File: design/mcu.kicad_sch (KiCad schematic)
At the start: 13 parts, among them U1 STM32F40X_LQFP64, X1 8MHz

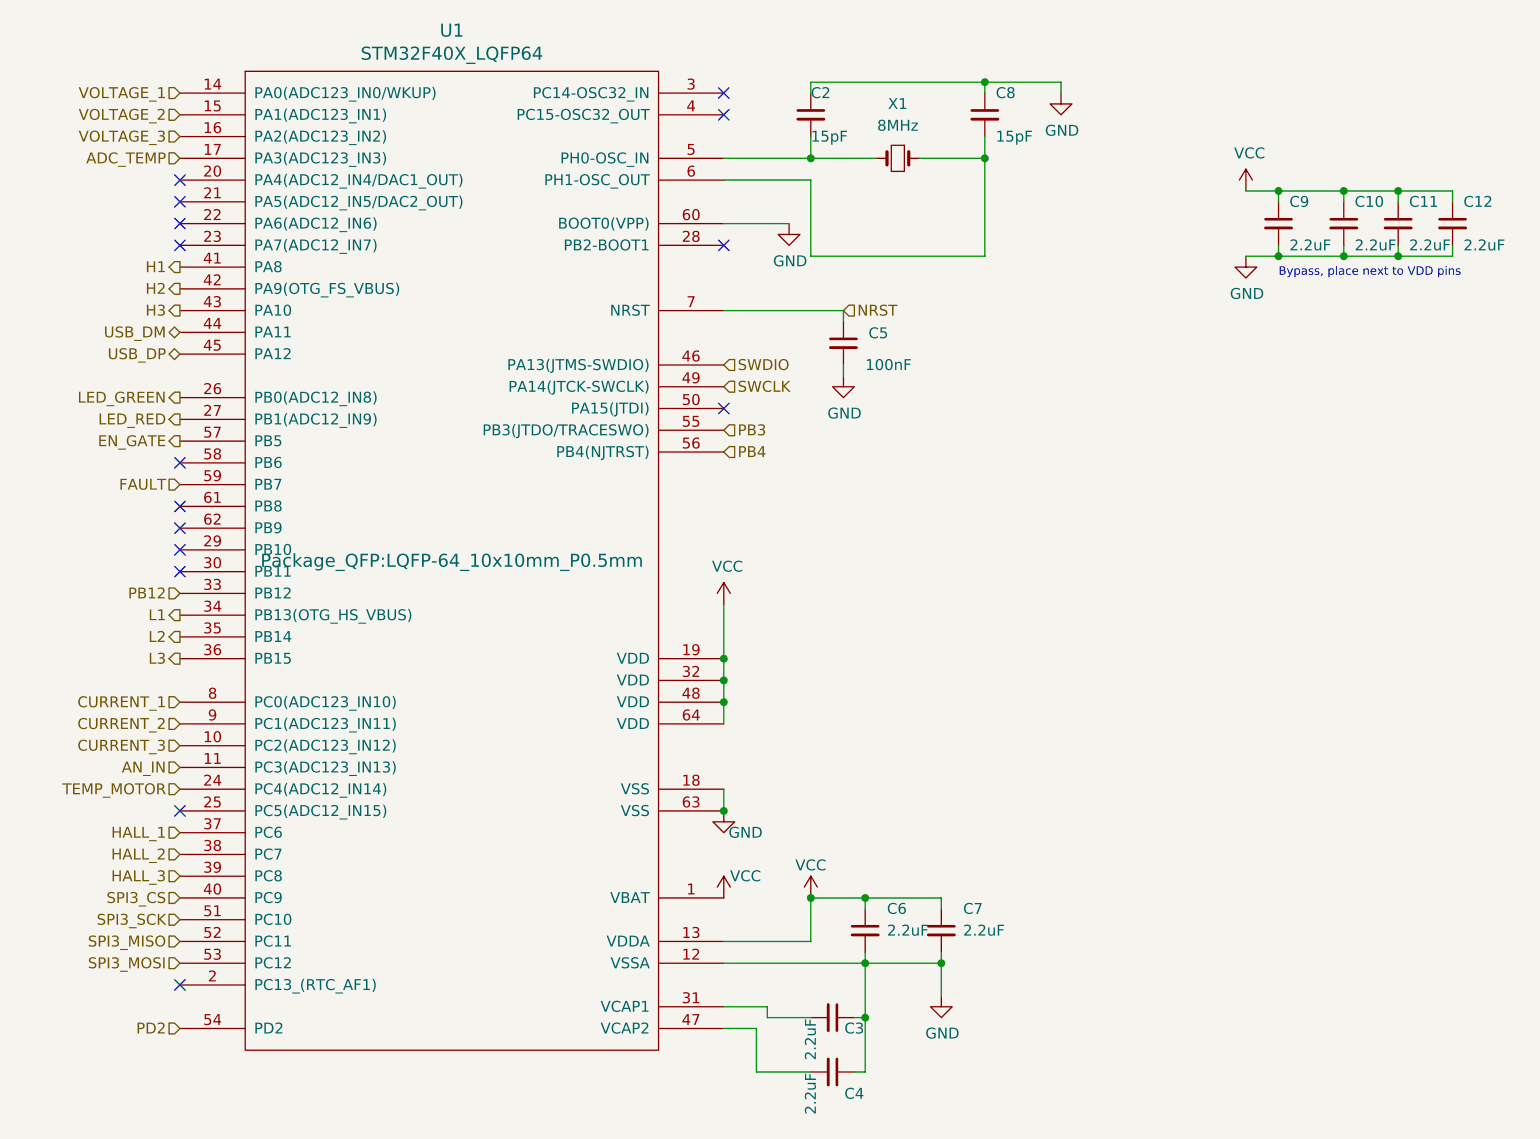
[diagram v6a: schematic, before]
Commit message: Ordenado del esquemático
- Cambios en los capacitores del oscilador
- Mejora de los esquemáticos, encapsulado la interfáz usb y los sensores del motor
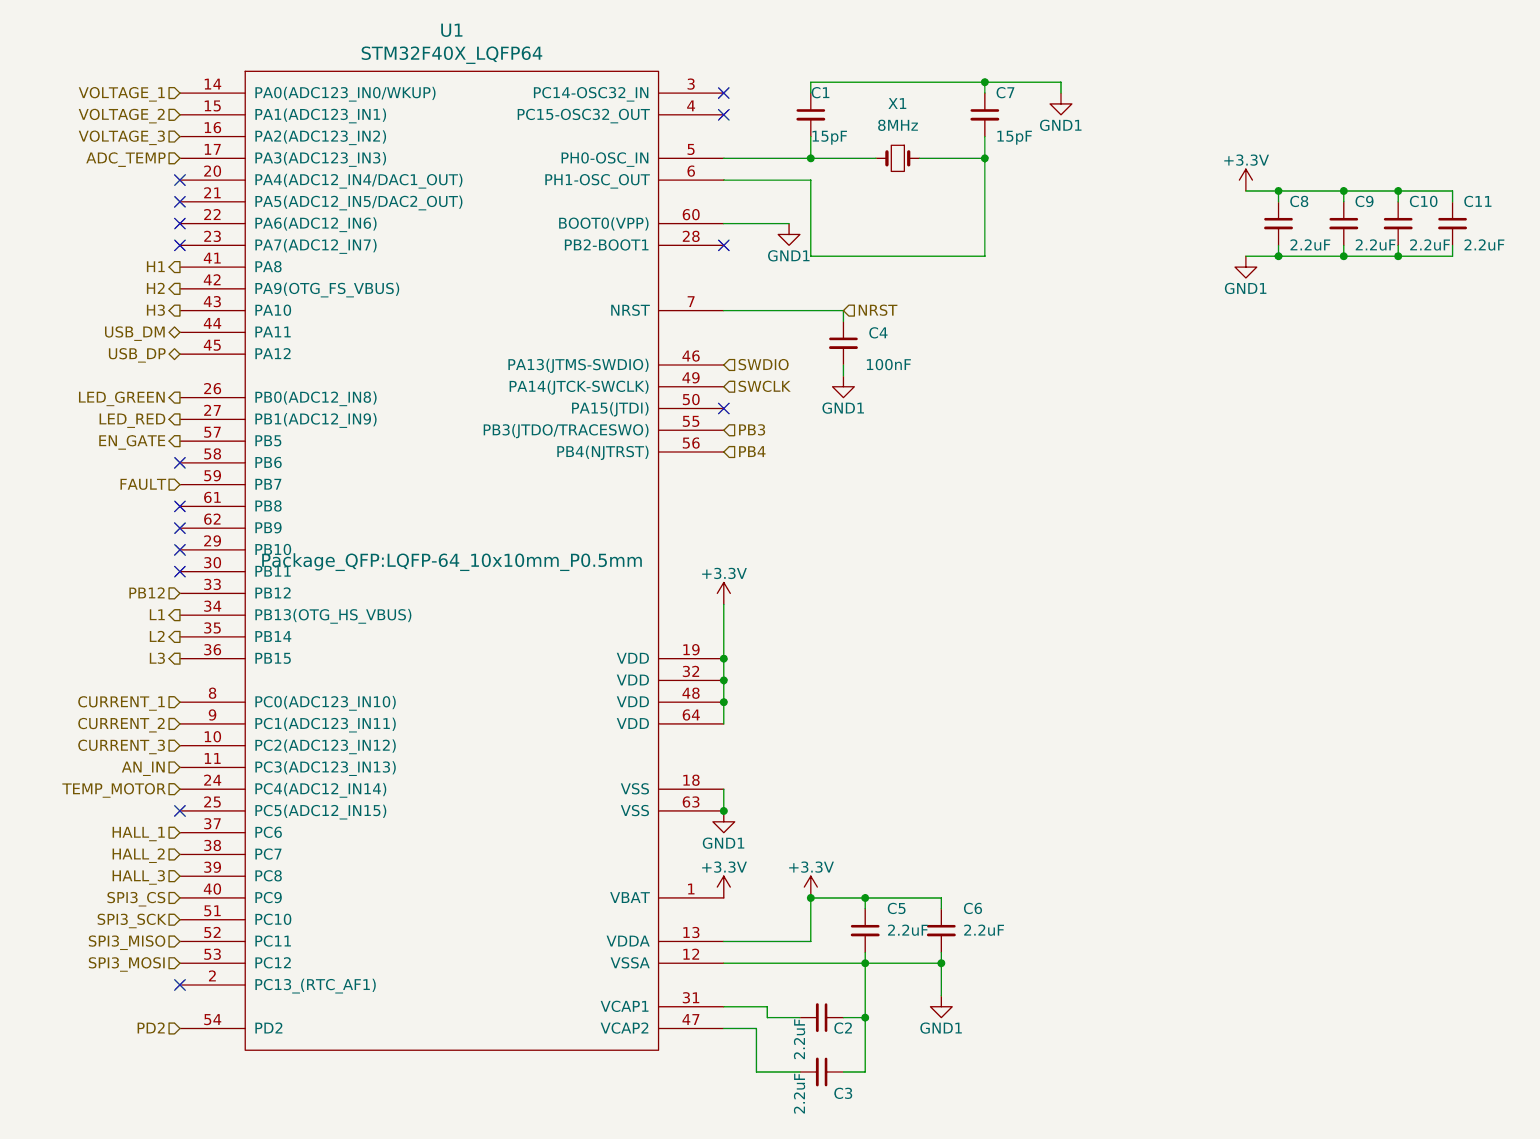
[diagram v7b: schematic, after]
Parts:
- renumbered C2 to C1, C11 to C10, C12 to C11, C3 to C2, C4 to C3, C5 to C4, C6 to C5, C7 to C6, C8 to C7, C9 to C8, C10 to C9
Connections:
- net GND renamed GND1
- net VCC renamed +3.3V
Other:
- note removed: "Bypass, place next to VDD pins"
- moved on the sheet: C2, C3

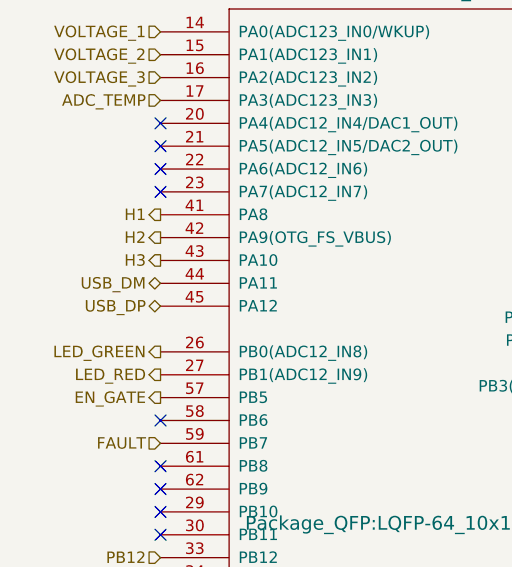
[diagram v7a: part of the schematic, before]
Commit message: Rotado del driver
Rotado del driver, cambiado de capacitores, disipación de transistores, cambiado de capacitores de semi puentes.
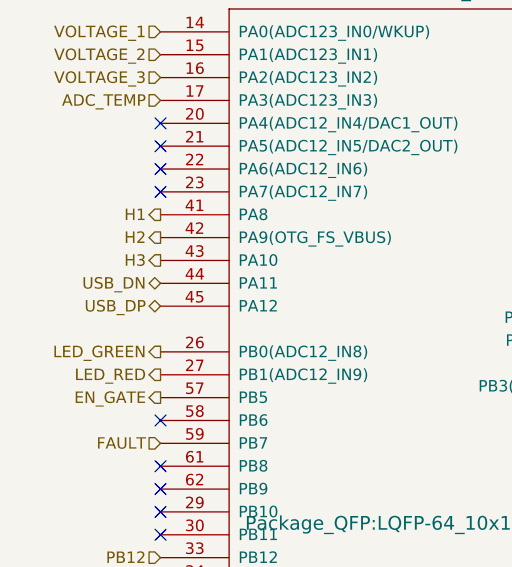
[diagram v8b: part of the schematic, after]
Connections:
- net USB_DM renamed USB_DN
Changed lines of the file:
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@@
 		)
 	)
-	(hierarchical_label "USB_DM"
+	(hierarchical_label "USB_DN"
 		(shape bidirectional)
 		(at 121.92 59.69 180)
